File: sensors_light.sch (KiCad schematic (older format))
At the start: 6 parts

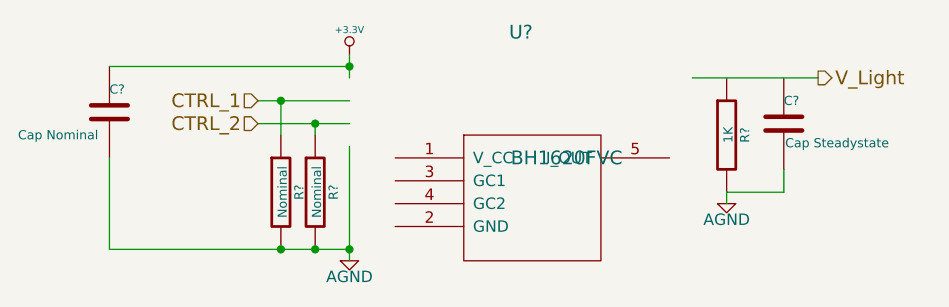
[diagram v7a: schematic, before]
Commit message: added missing datasheets to old components
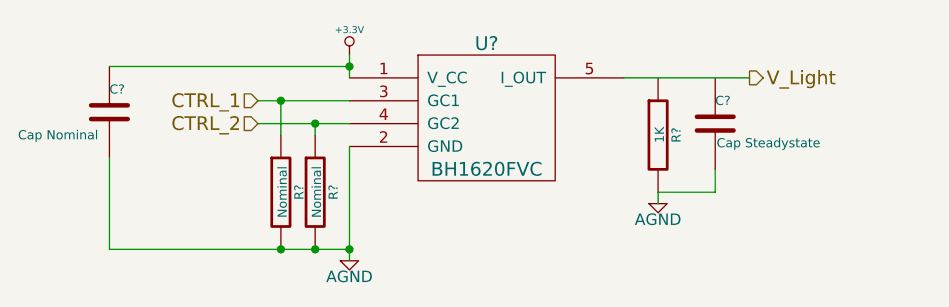
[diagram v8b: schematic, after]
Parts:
- removed U?: BH1620FVC, ~, symbol BH1620FVC
- added U?: BH1620FVC, ~, symbol BH1620FVC
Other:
- moved on the sheet: C?, R?
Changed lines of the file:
@@
 L R R?
 U 1 1 527B1F07
-P 4600 1050
-F 0 "R?" V 4680 1050 40  0000 C CNN
-F 1 "1K" V 4607 1051 40  0000 C CNN
-F 2 "~" V 4530 1050 30  0000 C CNN
-F 3 "~" H 4600 1050 30  0000 C CNN
-	1    4600 1050
+P 4300 1050
+F 0 "R?" V 4380 1050 40  0000 C CNN
+F 1 "1K" V 4307 1051 40  0000 C CNN
+F 2 "~" V 4230 1050 30  0000 C CNN
+F 3 "~" H 4300 1050 30  0000 C CNN
+	1    4300 1050
 	1    0    0    -1
 $EndComp
@@
 L C C?
 U 1 1 527B20AA
-P 4850 1000
-F 0 "C?" H 4850 1100 40  0000 L CNN
-F 1 "Cap Steadystate" H 4856 915 40  0000 L CNN
-F 2 "~" H 4888 850 30  0000 C CNN
-F 3 "~" H 4850 1000 60  0000 C CNN
-	1    4850 1000
+P 4550 1000
+F 0 "C?" H 4550 1100 40  0000 L CNN
+F 1 "Cap Steadystate" H 4556 915 40  0000 L CNN
+F 2 "~" H 4588 850 30  0000 C CNN
+F 3 "~" H 4550 1000 60  0000 C CNN
+	1    4550 1000
 	1    0    0    -1
 $EndComp
@@
 	1    0    0    -1
 $EndComp
-Text HLabel 5000 800  2    60   Output ~ 0
+Text HLabel 4700 800  2    60   Output ~ 0
 V_Light
-$Comp
-L BH1620FVC U?
-U 1 1 527B212A
-P 3750 1000
-F 0 "U?" H 3700 1400 60  0000 C CNN
-F 1 "BH1620FVC" H 3900 850 60  0000 C CNN
-F 2 "~" H 3450 1400 60  0000 C CNN
-F 3 "~" H 3450 1400 60  0000 C CNN
-	1    3750 1000
-	1    0    0    -1
-$EndComp
 $Comp
 L AGND #PWR?
@@
 L AGND #PWR?
 U 1 1 527B22C6
-P 4600 1350
-F 0 "#PWR?" H 4600 1350 40  0001 C CNN
-F 1 "AGND" H 4600 1280 50  0000 C CNN
-F 2 "" H 4600 1350 60  0000 C CNN
-F 3 "" H 4600 1350 60  0000 C CNN
-	1    4600 1350
+P 4300 1350
+F 0 "#PWR?" H 4300 1350 40  0001 C CNN
+F 1 "AGND" H 4300 1280 50  0000 C CNN
+F 2 "" H 4300 1350 60  0000 C CNN
+F 3 "" H 4300 1350 60  0000 C CNN
+	1    4300 1350
 	1    0    0    -1
 $EndComp
@@
 CTRL_2
 Wire Wire Line
-	4450 800  5000 800
+	4150 800  4700 800
 Wire Wire Line
 	2950 1100 2950 1550
@@
 	2950 750  2950 800
 Wire Wire Line
-	4600 1300 4600 1350
+	4300 1300 4300 1350
 Wire Wire Line
 	1900 750  2950 750
@@
 Connection ~ 2650 1550
 Wire Wire Line
-	4600 1300 4850 1300
+	4300 1300 4550 1300
 Wire Wire Line
-	4850 1300 4850 1200
+	4550 1300 4550 1200
+$Comp
+L BH1620FVC U?
+U 1 1 529265A6
+P 3550 650
+F 0 "U?" H 3550 650 60  0000 C CNN
+F 1 "BH1620FVC" H 3550 100 60  0000 C CNN
+F 2 "~" H 3250 1050 60  0000 C CNN
+F 3 "~" H 3250 1050 60  0000 C CNN
+	1    3550 650
+	1    0    0    -1
+$EndComp
 $EndSCHEMATC
